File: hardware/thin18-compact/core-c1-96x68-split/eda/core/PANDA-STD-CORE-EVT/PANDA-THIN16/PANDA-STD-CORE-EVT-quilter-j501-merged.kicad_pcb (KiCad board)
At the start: 4 copper layers, 96 x 68 mm, 149 parts, among them J201 U20405-01 USB2.0, J301 DF58-2P-1.2V(21), J302 HC-1.0-3PWT NTC, J501 104031-0811 / microSD, J502 HC-1.0-2PWT BTL, J503 TC2030-IDC-NL / DEBUG, J601 HC-PBB40C-60DS-0.4V-1.5-02, J803 X05A10H06G, J804 X05A10H06G, SW201 TS-1186E-B-B, SW202 TS-1186E-B-B, U302 RV-3028-C7, U402 SGM2578SDYG/TR, U403 SGM2578SDYG/TR, U404 SGM2578SDYG/TR, U405 SGM2578SDYG/TR, U501 ESP32-S3-WROOM-1U-N16R8, U503 QMI8658A, U601 XL9535, U901 SGM41513YTQF24G/TR, U902 SGM62125AXG/TR, U903 CW2217BAAD, U904 NS4168, U905 SGM37601YTRL20G/TR

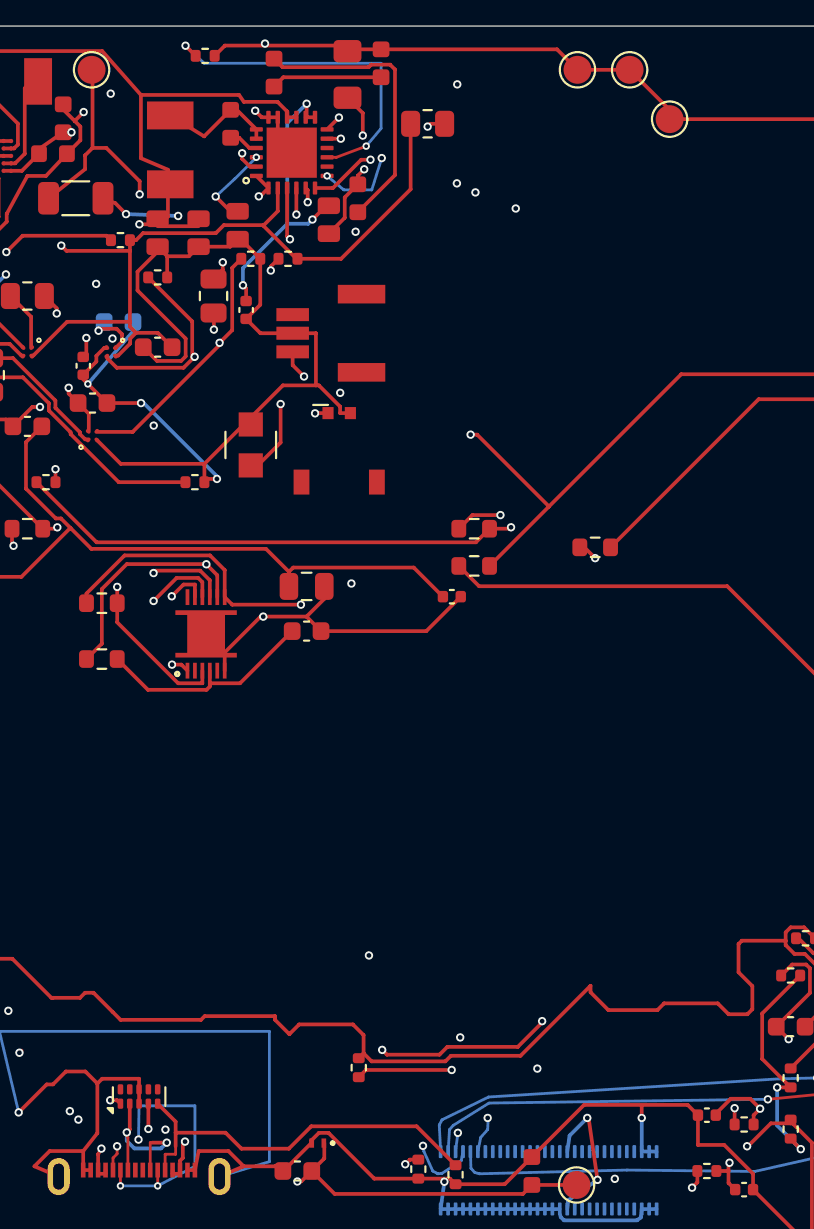
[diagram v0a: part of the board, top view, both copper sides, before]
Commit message: hardware: close three imported Split-C1 refs and two SMT maps
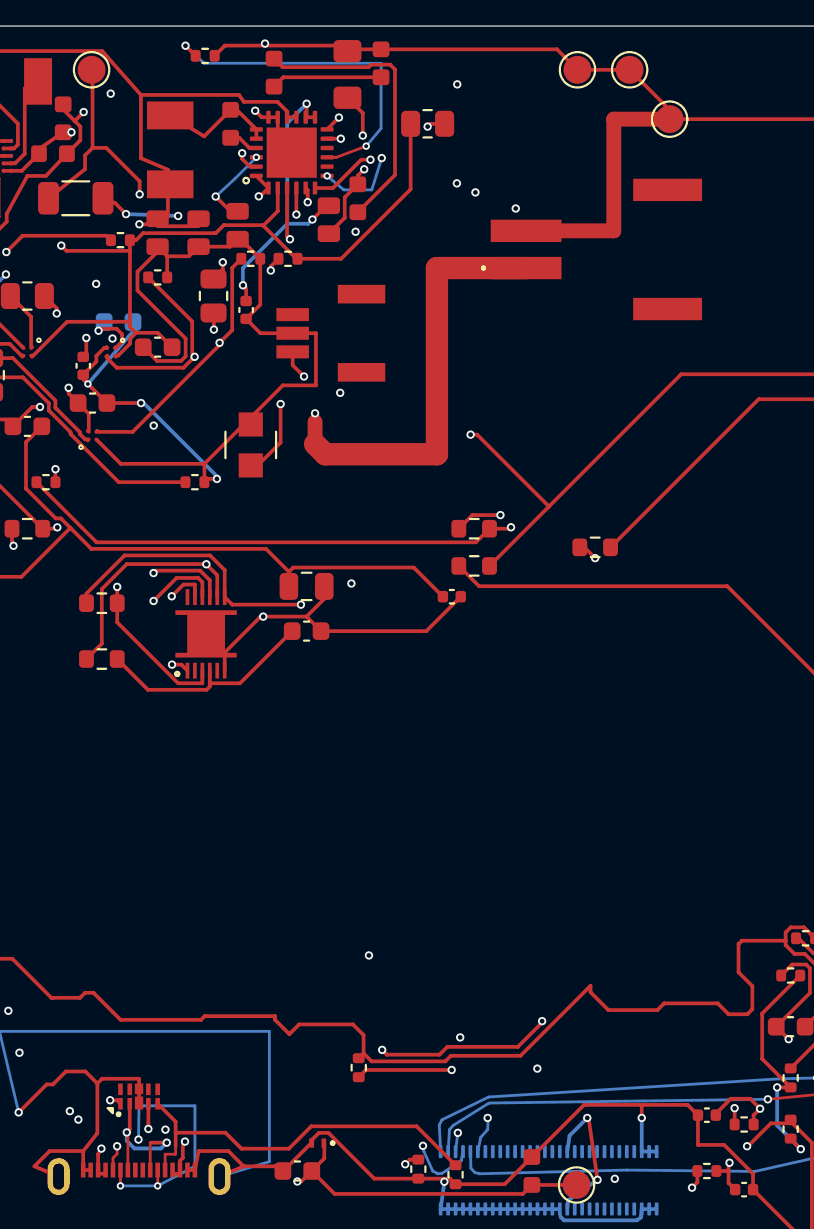
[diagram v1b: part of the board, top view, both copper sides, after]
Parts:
- D201: value TPD4E05U06DQAR -> LRC8804FDT1G; footprint Package_SON:USON-10_2.5x1.0mm_P0.5mm -> panda-standard:LRC8804F_DFN2510
- J301: value DF58-2P-1.2V(21) -> HC-HY-2AWT; footprint panda-battery:Hirose_DF58-2P-1.2V_1x02_P1.2mm_Vertical -> panda-standard:HCTL_HC_HY_2AWT
- moved J301 16.5 mm to (62.0, 12.0), turned to 90 degrees
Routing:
- net BAT_CONN_P: track 52.5 -> 75.0 mm
- net GND: track 732.9 -> 743.9 mm

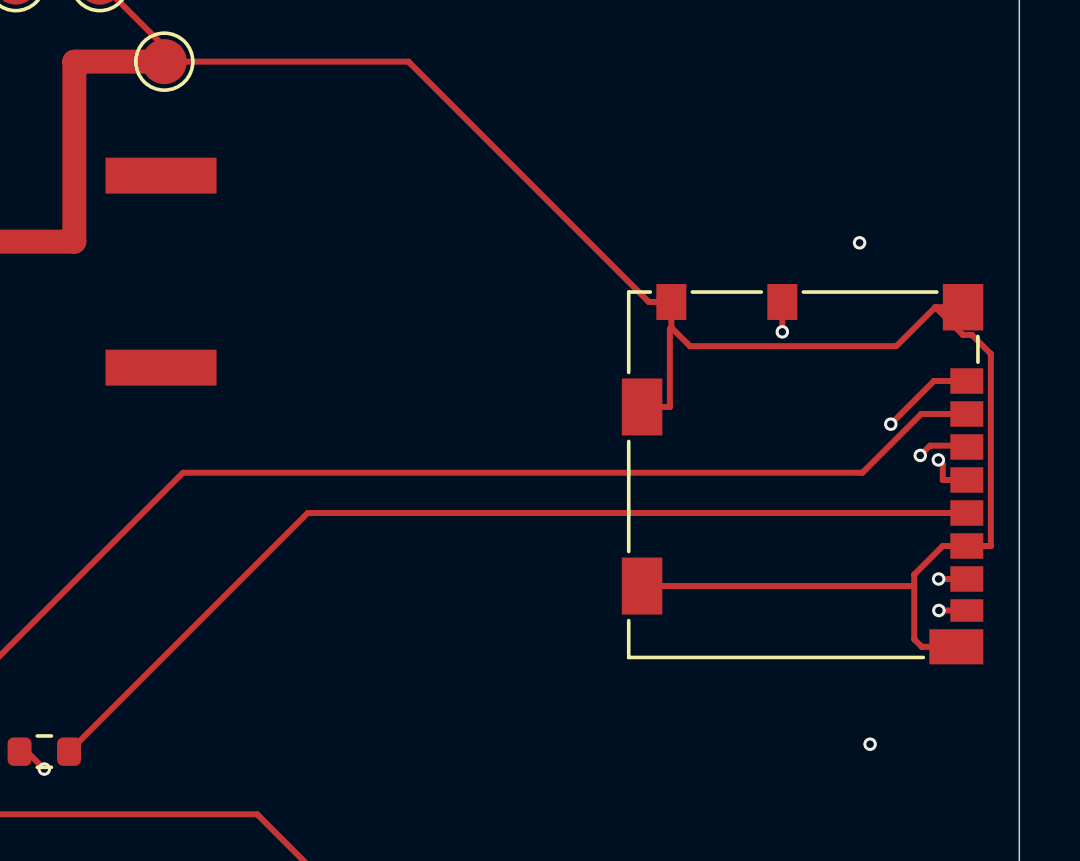
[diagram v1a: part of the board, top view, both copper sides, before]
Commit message: hw: apply XUNPU microSD and reviewed Sunlord MT inductor ECOs
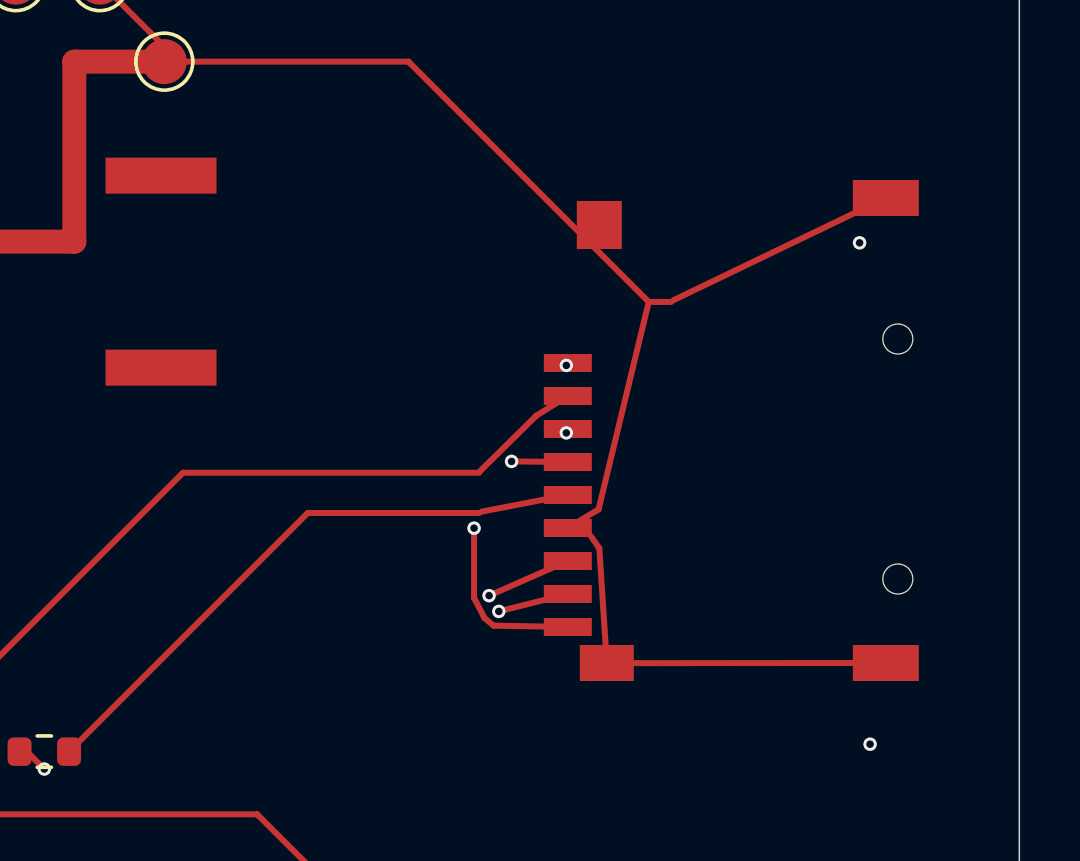
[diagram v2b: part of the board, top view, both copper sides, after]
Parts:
- J501: value 104031-0811 / microSD -> TF-122-CCP9 / microSD; footprint Connector_Card:microSD_HC_Molex_104031-0811 -> panda-standard:XUNPU_TF_122_CCP9
- L402: footprint panda-standard:Sunlord_MWSA0402_1R0B01 -> panda-standard:Sunlord_MWSA0402_1R0
- moved J501 7.19 mm to (81.8, 17.3), turned to 90 degrees
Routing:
- net SDMMC_CMD_CARD: track 81.2 -> 66.7 mm
- net SDMMC_D0_CARD: track 71.3 -> 57.9 mm
- net SDMMC_CLK_CARD: track 33.2 -> 19.9 mm
- net SDMMC_D1_CARD: track 63.9 -> 50.6 mm
- net SDMMC_D3_CARD: track 89.2 -> 75.9 mm
- net 3V3_SD: track 135.4 -> 123.1 mm
- net SDMMC_D2_CARD: track 93.5 -> 82.3 mm
- net GND: track 743.9 -> 733.2 mm
- net SD_CD: track 85.6 -> 80.8 mm

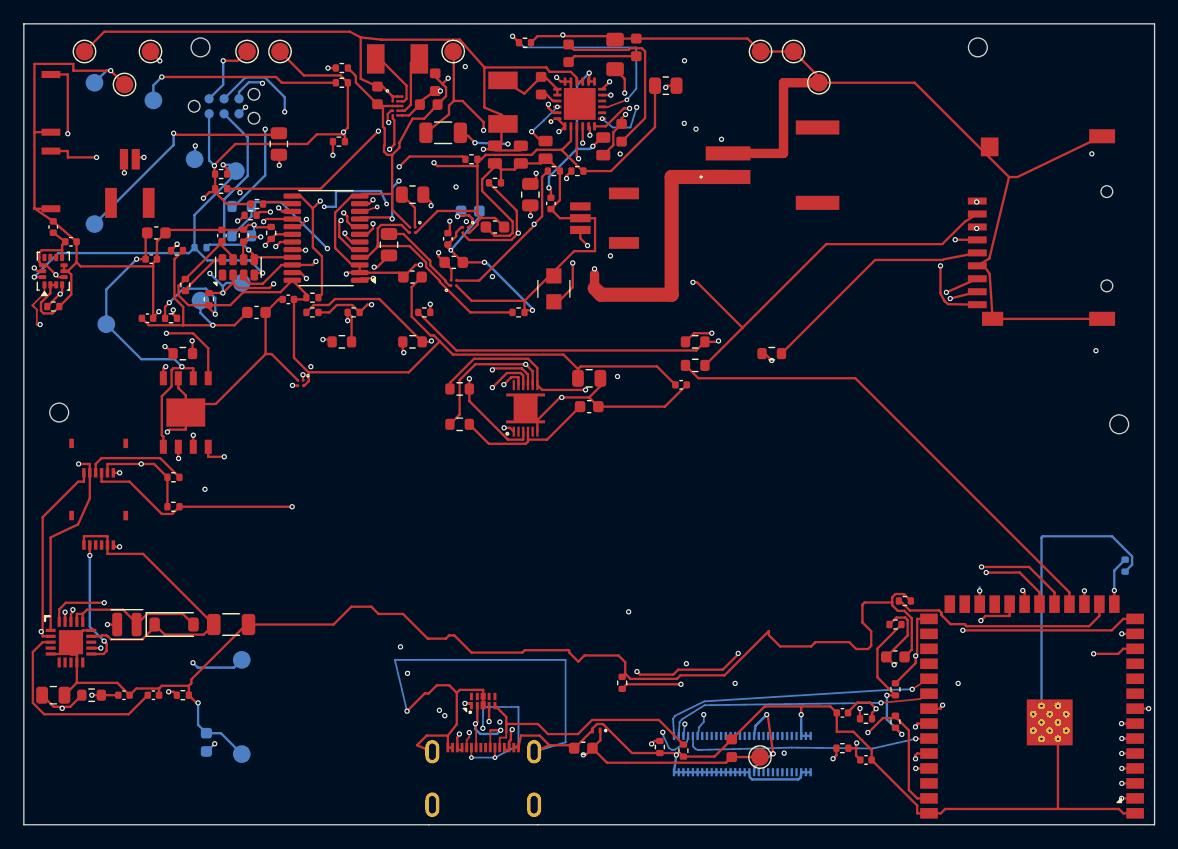
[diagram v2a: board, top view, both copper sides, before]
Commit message: hw: complete Split-C1 domestic RTC backup and EPD MOS ECO
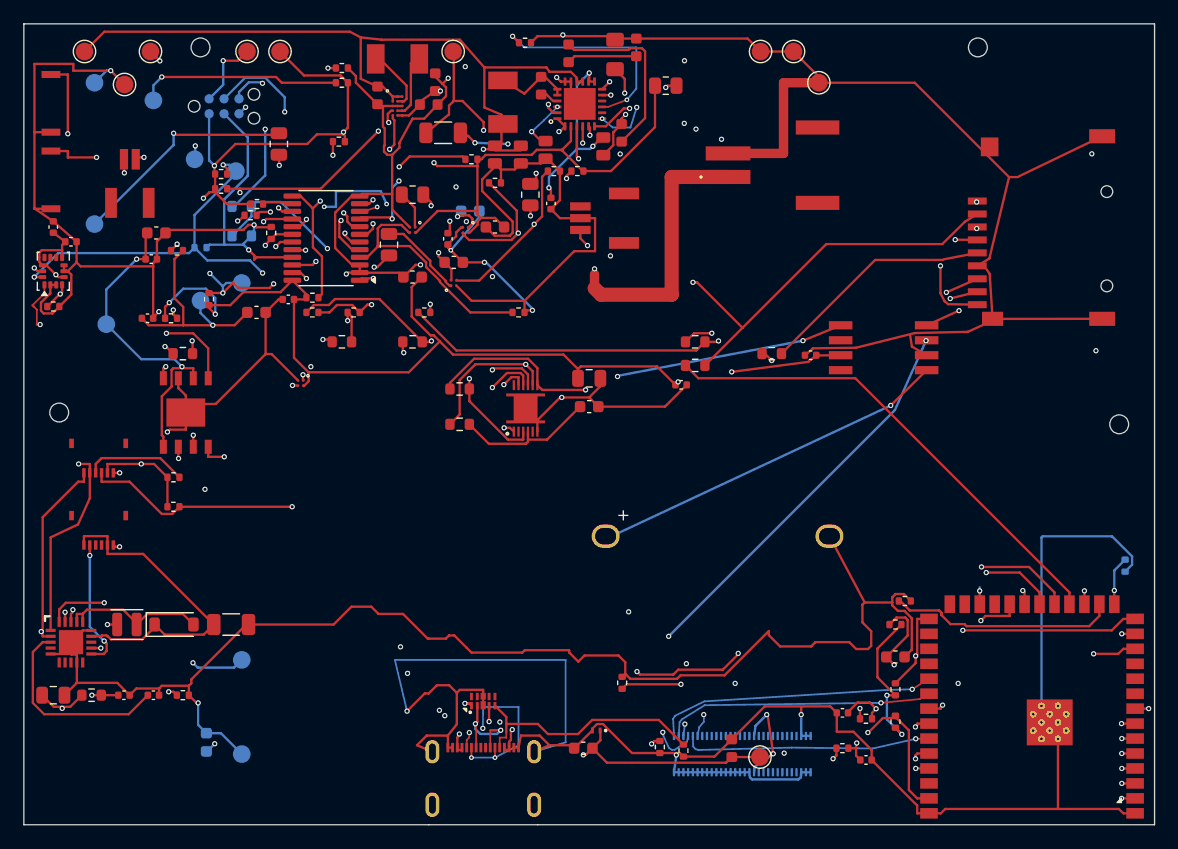
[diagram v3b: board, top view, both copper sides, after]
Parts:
- removed R303: 10k / RTC EVI PU, Resistor_SMD:R_0402_1005Metric
- removed R304: 10k / VBACKUP no-backup / DNP with C301, Resistor_SMD:R_0402_1005Metric
- C301: value CPH3225A 11mF 3.3V RTC backup candidate -> SE-5R5-D105VYH; footprint panda-standard:CPH3225A_Polarized_Derived -> panda-standard:KAMCAP_SE5R5_D105VYH
- U302: value RV-3028-C7 -> SD3078; footprint Package_SON:MicroCrystal_C7_SON-8_1.5x3.2mm_P0.9mm -> panda-standard:WAVE_SD3078_SOP8_208mil
- moved U302 55.2 mm to (73.0, 27.5), turned to 0 degrees
- moved C302 51.0 mm to (66.8, 28.1), turned to 180 degrees
- moved C301 25.2 mm to (58.9, 43.5), turned to 0 degrees
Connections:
- U302 pad 1: unconnected-(U302-CLKOUT-Pad1) -> I2C_SCL
- U302 pad 2: EXP_INT -> unconnected-(U302-F32K-Pad2)
- U302 pad 3: I2C_SCL -> 3V3_AON
- U302 pad 4: I2C_SDA -> unconnected-(U302-NC-Pad4)
- U302 pad 5: GND -> RTC_VBACKUP
- U302 pad 6: RTC_VBACKUP -> GND
- U302 pad 7: 3V3_AON -> EXP_INT
- U302 pad 8: RTC_EVI -> I2C_SDA
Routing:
- net EXP_INT: track 141.3 -> 174.3 mm, vias 7 -> 9
- net GND: track 733.2 -> 757.4 mm
- net I2C_SDA: track 238.0 -> 253.8 mm, vias 12 -> 13
- net I2C_SCL: track 247.5 -> 261.6 mm, vias 14 -> 15
- net RTC_VBACKUP: track 34.9 -> 29.7 mm, vias 2 -> 1
- net RTC_EVI: track 4.33 -> 0.00 mm
- net 3V3_AON: track 338.8 -> 341.9 mm, vias 12 -> 14
